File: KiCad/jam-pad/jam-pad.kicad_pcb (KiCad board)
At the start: 2 copper layers, 199.2 x 57.1 mm, 62 parts, among them J1 USB_C, J2 PH_01x03_2.54mm, SW1 MX_Hotswap, SW10 MX_Hotswap, SW11 MX_Hotswap, SW12 MX_Hotswap, SW13 SW_Push, SW14 RotaryEncoder_Switch, SW15 SW_Push, SW2 MX_Hotswap, SW3 MX_Hotswap, SW4 MX_Hotswap, SW5 MX_Hotswap, SW6 MX_Hotswap, SW7 MX_Hotswap, SW8 MX_Hotswap, SW9 MX_Hotswap, U1 RP2040, U2 OLED_RGB_128x128_waveshare, U3 W25Q16JVSNIQ, U4 MIC5319-3.3YD5, Y1 ECS-120-18-33-JGN

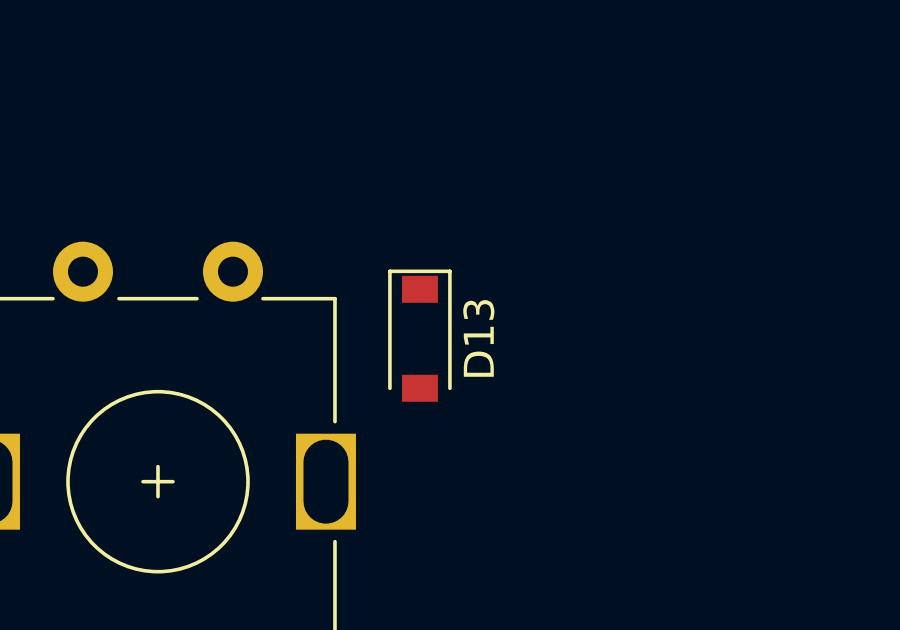
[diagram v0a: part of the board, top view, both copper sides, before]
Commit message: moved d13 to bottom
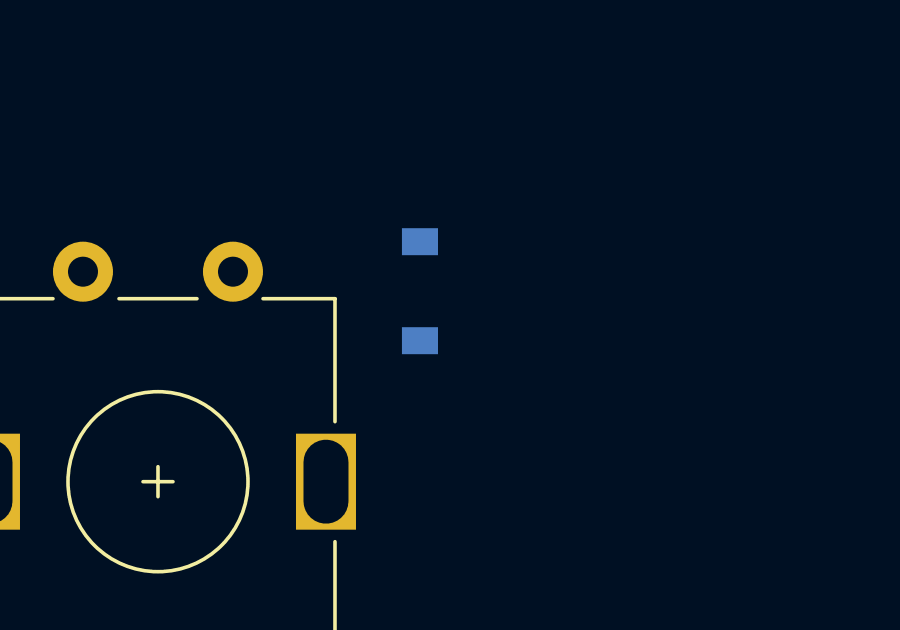
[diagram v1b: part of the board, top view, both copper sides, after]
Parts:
- D13: moved to B.Cu
- moved D13 1.59 mm to (65.1, 47.6)
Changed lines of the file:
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@@
-    )
-  )
-  (footprint "Diode_SMD:D_SOD-123" (layer "F.Cu")
-    (at 65.0875 49.2125 -90)
-    (descr "SOD-123")
-    (tags "SOD-123")
-    (property "Sheetfile" "jam-pad.kicad_sch")
-    (property "Sheetname" "")
-    (attr smd)
-    (fp_text reference "D13" (at 0 -2 90) (layer "F.SilkS")
-      (effects (font (size 1 1) (thickness 0.15)))
-    )
-    (fp_text value "1N4148W" (at 0 2.1 90) (layer "F.Fab")
-      (effects (font (size 1 1) (thickness 0.15)))
-    )
-    (fp_text user "${REFERENCE}" (at 0 -2 90) (layer "F.Fab")
-      (effects (font (size 1 1) (thickness 0.15)))
-    )
-    (fp_line (start -2.25 -1) (end 1.65 -1) (layer "F.SilkS") (width 0.12))
-    (fp_line (start -2.25 1) (end 1.65 1) (layer "F.SilkS") (width 0.12))
-    (fp_line (start -2.25 -1) (end -2.25 1) (layer "F.SilkS") (width 0.12))
-    (fp_line (start 2.35 1.15) (end -2.35 1.15) (layer "F.CrtYd") (width 0.05))
-    (fp_line (start -2.35 -1.15) (end 2.35 -1.15) (layer "F.CrtYd") (width 0.05))
-    (fp_line (start 2.35 -1.15) (end 2.35 1.15) (layer "F.CrtYd") (width 0.05))
-    (fp_line (start -2.35 -1.15) (end -2.35 1.15) (layer "F.CrtYd") (width 0.05))
-    (fp_line (start 1.4 0.9) (end -1.4 0.9) (layer "F.Fab") (width 0.1))
-    (fp_line (start -0.35 0) (end -0.35 0.55) (layer "F.Fab") (width 0.1))
-    (fp_line (start 0.25 0.4) (end -0.35 0) (layer "F.Fab") (width 0.1))
-    (fp_line (start 0.25 0) (end 0.75 0) (layer "F.Fab") (width 0.1))
-    (fp_line (start -0.35 0) (end -0.35 -0.55) (layer "F.Fab") (width 0.1))
-    (fp_line (start 0.25 -0.4) (end 0.25 0.4) (layer "F.Fab") (width 0.1))
-    (fp_line (start 1.4 -0.9) (end 1.4 0.9) (layer "F.Fab") (width 0.1))
-    (fp_line (start -0.35 0) (end 0.25 -0.4) (layer "F.Fab") (width 0.1))
-    (fp_line (start -1.4 0.9) (end -1.4 -0.9) (layer "F.Fab") (width 0.1))
-    (fp_line (start -0.75 0) (end -0.35 0) (layer "F.Fab") (width 0.1))
-    (fp_line (start -1.4 -0.9) (end 1.4 -0.9) (layer "F.Fab") (width 0.1))
-    (pad "1" smd rect (at -1.65 0 270) (size 0.9 1.2) (layers "F.Cu" "F.Paste" "F.Mask")
-      (net 8 "Row0") (pinfunction "K") (pintype "passive"))
-    (pad "2" smd rect (at 1.65 0 270) (size 0.9 1.2) (layers "F.Cu" "F.Paste" "F.Mask")
-      (net 23 "Net-(D13-Pad2)") (pinfunction "A") (pintype "passive"))
-    (model "${KICAD6_3DMODEL_DIR}/Diode_SMD.3dshapes/D_SOD-123.wrl"
-      (offset (xyz 0 0 0))
-      (scale (xyz 1 1 1))
-      (rotate (xyz 0 0 0))
     )
   )
@@
     (model "${KICAD6_3DMODEL_DIR}/Diode_SMD.3dshapes/D_SOD-123.wrl"
       (offset (xyz 0 0 0))
+      (scale (xyz 1 1 1))
+      (rotate (xyz 0 0 0))
+    )
+  )
+  (footprint "Diode_SMD:D_SOD-123" (layer "B.Cu")
+    (at 65.0875 47.625 -90)
+    (descr "SOD-123")
+    (tags "SOD-123")
+    (property "Sheetfile" "jam-pad.kicad_sch")
+    (property "Sheetname" "")
+    (attr smd)
+    (fp_text reference "D13" (at 0 2 90) (layer "B.SilkS")
+      (effects (font (size 1 1) (thickness 0.15)) (justify mirror))
+    )
+    (fp_text value "1N4148W" (at 0 -2.1 90) (layer "B.Fab")
+      (effects (font (size 1 1) (thickness 0.15)) (justify mirror))
+    )
+    (fp_text user "${REFERENCE}" (at 0 2 90) (layer "B.Fab")
+      (effects (font (size 1 1) (thickness 0.15)) (justify mirror))
+    )
+    (fp_line (start -2.25 1) (end 1.65 1) (layer "B.SilkS") (width 0.12))
+    (fp_line (start -2.25 -1) (end 1.65 -1) (layer "B.SilkS") (width 0.12))
+    (fp_line (start -2.25 1) (end -2.25 -1) (layer "B.SilkS") (width 0.12))
+    (fp_line (start 2.35 -1.15) (end -2.35 -1.15) (layer "B.CrtYd") (width 0.05))
+    (fp_line (start -2.35 1.15) (end 2.35 1.15) (layer "B.CrtYd") (width 0.05))
+    (fp_line (start 2.35 1.15) (end 2.35 -1.15) (layer "B.CrtYd") (width 0.05))
+    (fp_line (start -2.35 1.15) (end -2.35 -1.15) (layer "B.CrtYd") (width 0.05))
+    (fp_line (start 1.4 -0.9) (end -1.4 -0.9) (layer "B.Fab") (width 0.1))
+    (fp_line (start -0.35 0) (end -0.35 -0.55) (layer "B.Fab") (width 0.1))
+    (fp_line (start 0.25 -0.4) (end -0.35 0) (layer "B.Fab") (width 0.1))
+    (fp_line (start 0.25 0) (end 0.75 0) (layer "B.Fab") (width 0.1))
+    (fp_line (start -0.35 0) (end -0.35 0.55) (layer "B.Fab") (width 0.1))
+    (fp_line (start 0.25 0.4) (end 0.25 -0.4) (layer "B.Fab") (width 0.1))
+    (fp_line (start 1.4 0.9) (end 1.4 -0.9) (layer "B.Fab") (width 0.1))
+    (fp_line (start -0.35 0) (end 0.25 0.4) (layer "B.Fab") (width 0.1))
+    (fp_line (start -1.4 -0.9) (end -1.4 0.9) (layer "B.Fab") (width 0.1))
+    (fp_line (start -0.75 0) (end -0.35 0) (layer "B.Fab") (width 0.1))
+    (fp_line (start -1.4 0.9) (end 1.4 0.9) (layer "B.Fab") (width 0.1))
+    (pad "1" smd rect (at -1.65 0 270) (size 0.9 1.2) (layers "B.Cu" "B.Paste" "B.Mask")
+      (net 8 "Row0") (pinfunction "K") (pintype "passive"))
+    (pad "2" smd rect (at 1.65 0 270) (size 0.9 1.2) (layers "B.Cu" "B.Paste" "B.Mask")
+      (net 23 "Net-(D13-Pad2)") (pinfunction "A") (pintype "passive"))
+    (model "${KICAD6_3DMODEL_DIR}/Diode_SMD.3dshapes/D_SOD-123.wrl"
+      (offset (xyz 0 0 0))

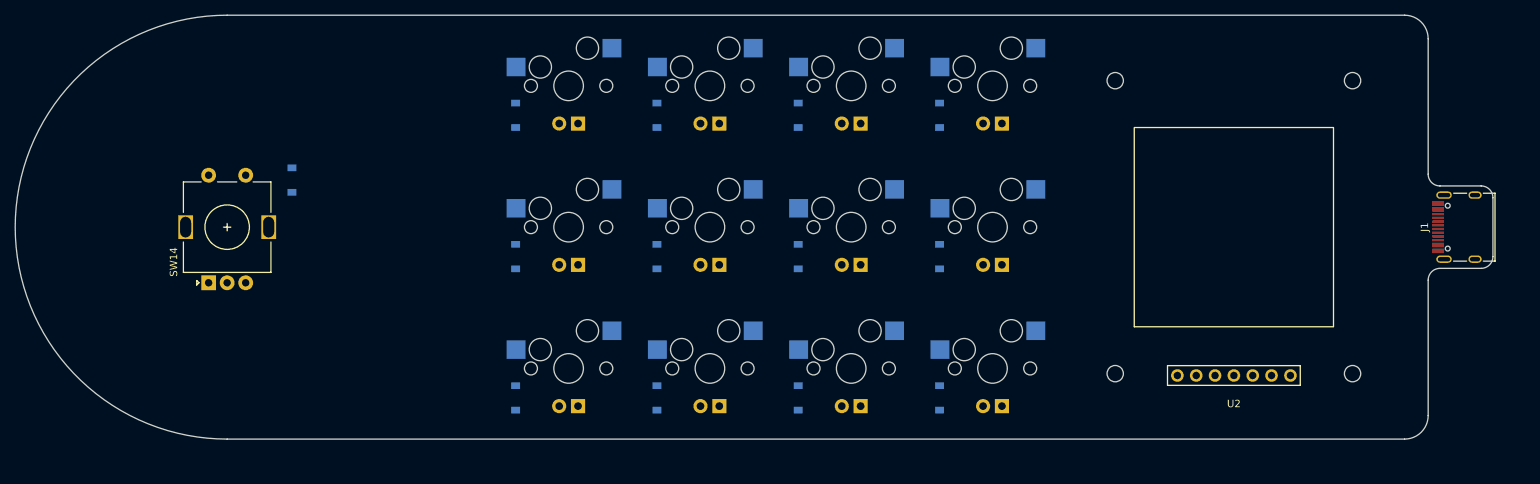
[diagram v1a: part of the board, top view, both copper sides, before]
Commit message: 12 to 9 keys
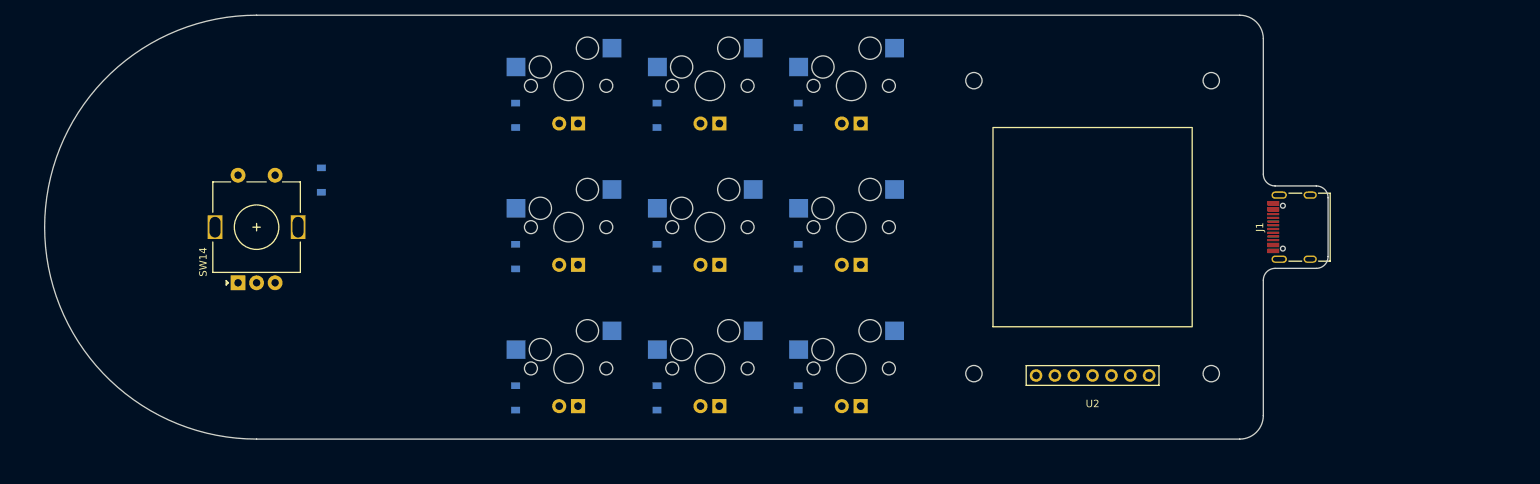
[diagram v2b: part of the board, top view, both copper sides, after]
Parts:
- removed D12: 1N4148W, Diode_SMD:D_SOD-123
- removed the D4 at (152.4, 38.9)
- removed the D8 at (152.4, 57.9)
- removed SW12: MX_Hotswap, MX_Only:MXOnly-1U-Hotswap-LED
- removed the SW4 at (159.5, 34.9)
- removed the SW8 at (159.5, 54.0)
- moved J1 22.2 mm to (198.2, 54.0)
- moved U2 19.1 mm to (173.0, 54.0)
- moved D13 3.97 mm to (69.1, 47.6)
- moved SW14 3.97 mm to (60.3, 54.0)
- renumbered D5 to D4, D6 to D5, D7 to D6, D9 to D7, D10 to D8, D11 to D9, SW5 to SW4, SW6 to SW5, SW7 to SW6, SW9 to SW7, SW10 to SW8, SW11 to SW9
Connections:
- SW14 pad S2: Col4 -> Col0
- U1 pad 11: /MOSI -> /SCLK
- U1 pad 12: /SCLK -> /CS
- U1 pad 13: /CS -> /DC
- U1 pad 14: /DC -> /OLED_RST
- U1 pad 15: /OLED_RST -> /ENC_A
- U1 pad 16: /ENC_A -> /ENC_C
- U1 pad 17: /ENC_C -> /ENC_B
- U1 pad 18: /ENC_B -> unconnected-(U1-Pad18)
- U1 pad 9: Col4 -> /MOSI
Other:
- board size 199.2 x 57.1 mm -> 173 x 57.1 mm

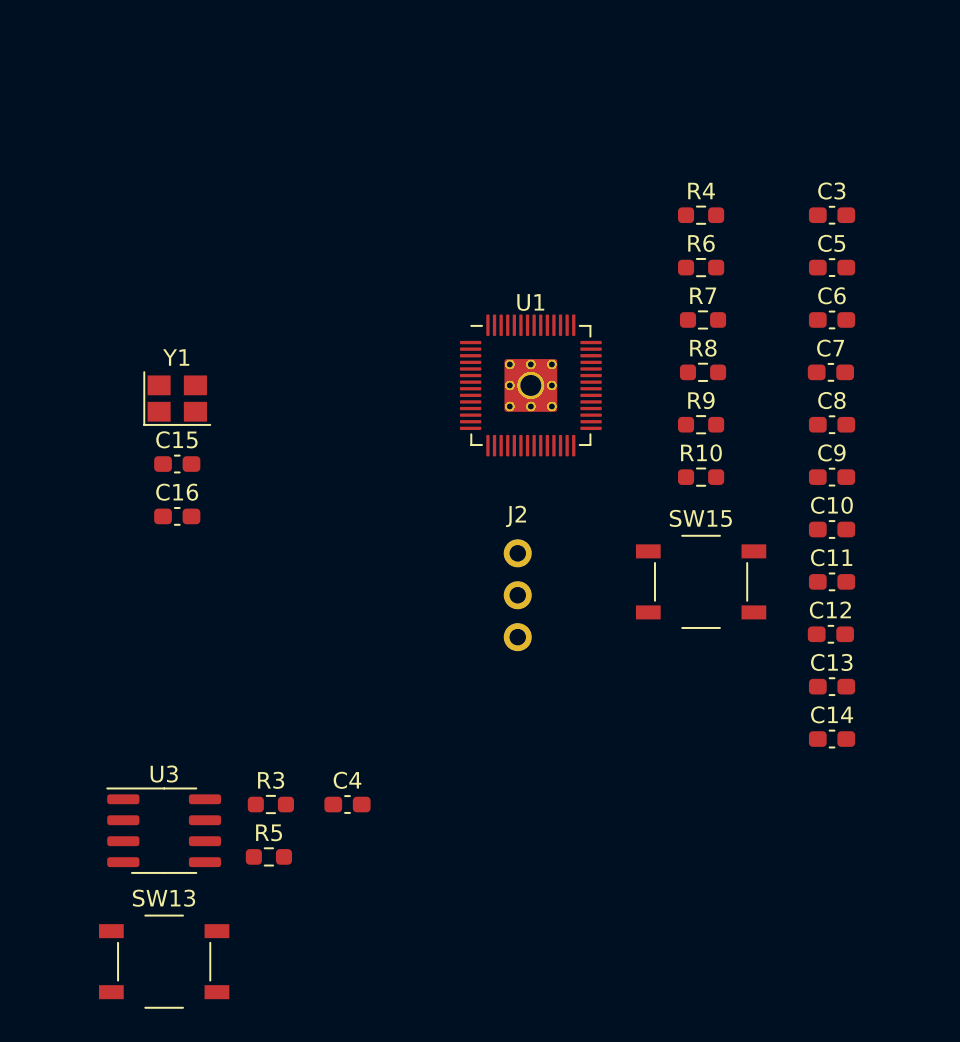
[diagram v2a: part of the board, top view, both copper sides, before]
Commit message: Place MCU parts
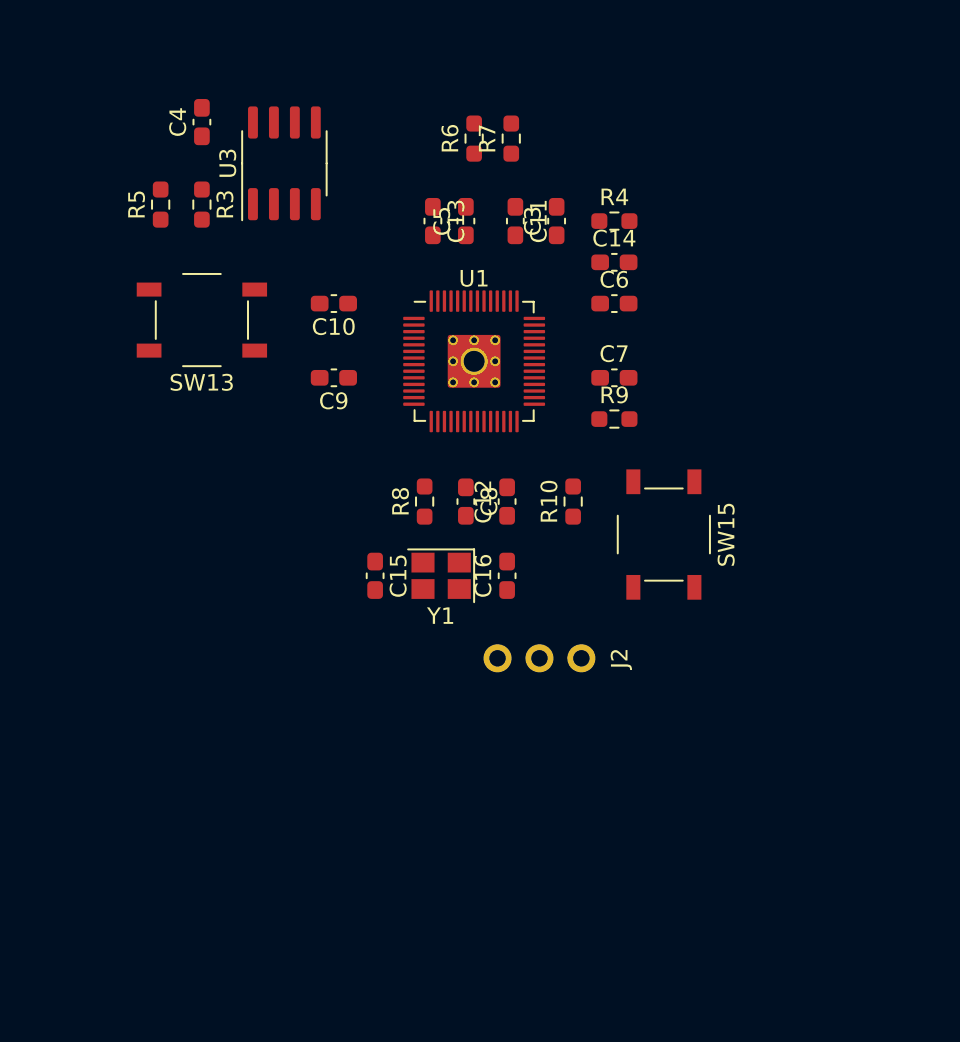
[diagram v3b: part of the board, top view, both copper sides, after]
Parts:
- moved C4 42.3 mm to (51.5, 128.5), turned to 90 degrees
- moved U3 41.1 mm to (56.5, 131.0), turned to 90 degrees
- moved R5 40.1 mm to (49.0, 133.5), turned to 90 degrees
- moved SW13 39.0 mm to (51.5, 140.5), turned to 180 degrees
- moved C13 37.2 mm to (65.5, 134.5), turned to -90 degrees
- moved R3 36.6 mm to (51.5, 133.5), turned to -90 degrees
- moved C10 33.2 mm to (59.5, 139.5), turned to 180 degrees
- moved C14 31.8 mm to (76.5, 137.0)
- moved C9 30.8 mm to (59.5, 144.0), turned to 180 degrees
- moved C11 29.1 mm to (70.5, 134.5), turned to -90 degrees
- moved C8 22.7 mm to (67.5, 151.5), turned to -90 degrees
- moved C5 22.4 mm to (67.5, 134.5), turned to 90 degrees
- moved C12 21.2 mm to (70.0, 151.5), turned to 90 degrees
- moved C16 20.3 mm to (70.0, 156.0), turned to 90 degrees
- moved Y1 19.3 mm to (66.0, 156.0), turned to 180 degrees
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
